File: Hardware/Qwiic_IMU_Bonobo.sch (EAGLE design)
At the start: 33 parts, among them J2 SMD, J3 PTH, J4 SMD, J6 SPI, U2 BNO080

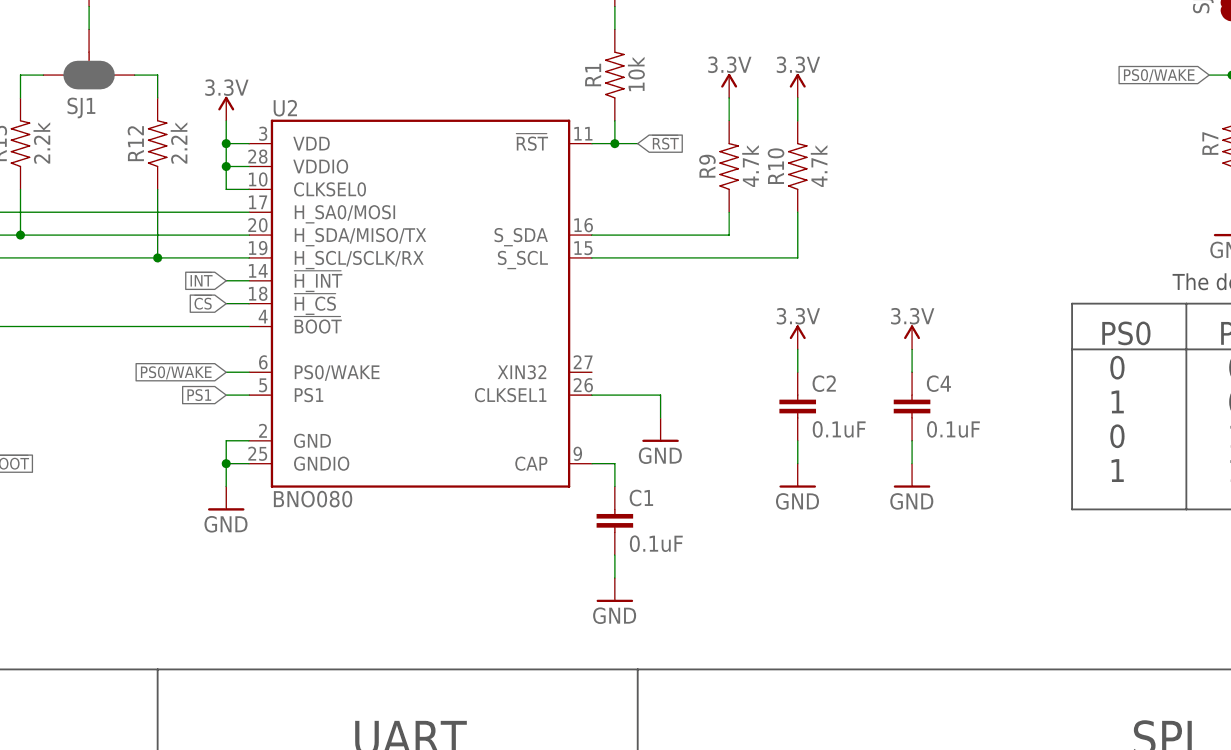
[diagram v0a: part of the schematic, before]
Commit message: Adding 32kHz xtal. Fixing UART silk.
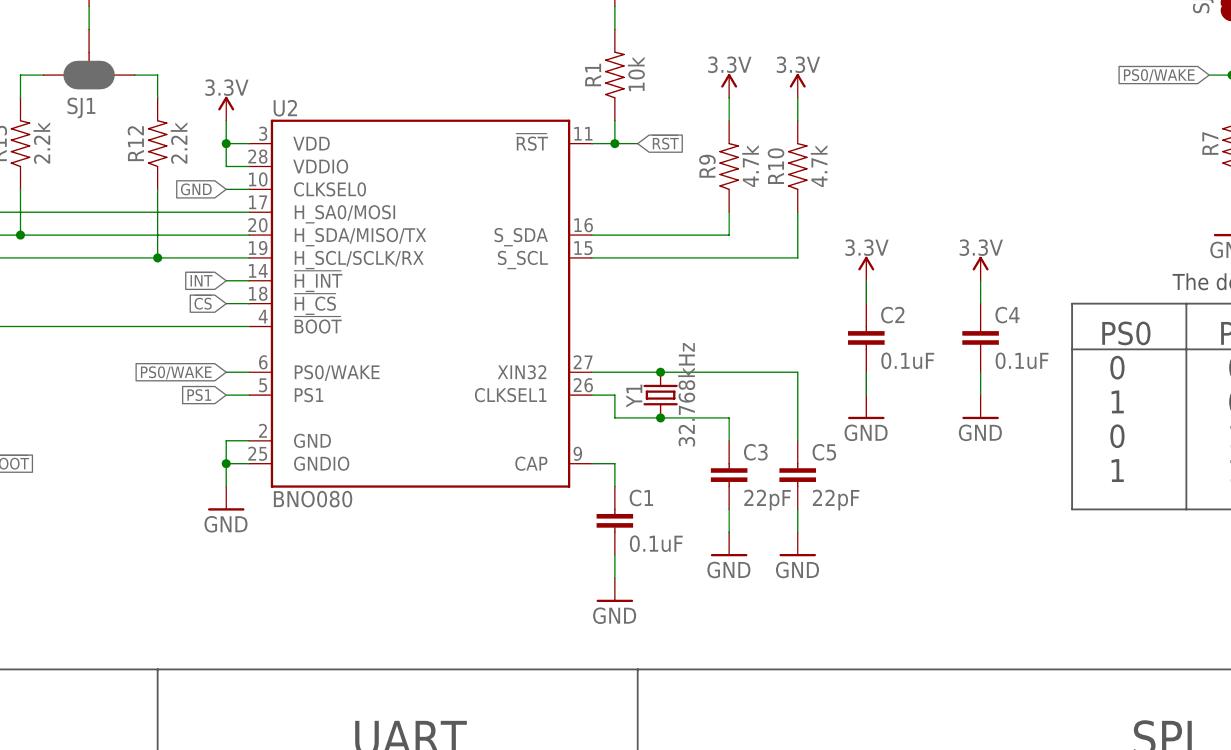
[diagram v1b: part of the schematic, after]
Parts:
- added C3, C5: 22pF, SparkFun-Capacitors:22PF-0603-50V-5%
- added Y1: 32.768kHz, SparkFun-Clocks:CRYSTAL-32.768KHZSMD-3.2X1.5
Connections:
- new net N$1: C5.1, U2.XIN32, Y1.2
- new net N$2: C3.1, U2.CLKSEL1, Y1.1
- net 3.3V: no longer U2.CLKSEL0
- net GND: now also C3.2, C5.2, U2.CLKSEL0; no longer U2.CLKSEL1
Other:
- moved on the sheet: C2, C4

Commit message: Label update. PWR LED added. Logo change.
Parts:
- removed U$1, U$2: SPARKX-LOGO3, SparkX:SPARKX-LOGO3
- added D1: RED, SparkFun-LED:LED-RED0603
- added LOGO4: SFE_LOGO_FLAME.1_INCH, SparkFun-Aesthetics:SFE_LOGO_FLAME.1_INCH
- added LOGO5: SFE_LOGO_NAME_FLAME.1_INCH, SparkFun-Aesthetics:SFE_LOGO_NAME_FLAME.1_INCH
- added R2: 1k, SparkFun-Resistors:1KOHM-0603-1/10W-1%
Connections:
- new net N$3: D1.C, R2.2
- net 3.3V: now also D1.A
- net GND: now also R2.1
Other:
- note added: "Power"
- moved on the sheet: R7, R8, SJ3, SJ4
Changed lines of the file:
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@@
 <part name="GND7" library="SparkFun" deviceset="GND" device=""/>
 <part name="FRAME1" library="SparkFun-Aesthetics" deviceset="FRAME-LETTER" device=""/>
-<part name="U$2" library="SparkX" deviceset="SPARKX-LOGO" device="3" value="SPARKX-LOGO3"/>
 <part name="C4" library="SparkFun-Capacitors" deviceset="0.1UF" device="-0603-25V-(+80/-20%)" value="0.1uF"/>
 <part name="SUPPLY8" library="SparkFun-PowerSymbols" deviceset="3.3V" device=""/>
@@
 <part name="GND8" library="SparkFun" deviceset="GND" device=""/>
 <part name="LOGO1" library="SparkFun-Aesthetics" deviceset="OSHW-LOGO" device="MINI"/>
-<part name="U$1" library="SparkX" deviceset="SPARKX-LOGO" device="3" value="SPARKX-LOGO3"/>
 <part name="U2" library="BNO080" deviceset="BNO080" device=""/>
 <part name="C1" library="SparkFun-Capacitors" deviceset="0.1UF" device="-0603-25V-(+80/-20%)" value="0.1uF"/>
@@
 <part name="C5" library="SparkFun-Capacitors" deviceset="22PF" device="-0603-50V-5%" value="22pF"/>
 <part name="GND14" library="SparkFun" deviceset="GND" device=""/>
+<part name="LOGO4" library="SparkFun-Aesthetics" deviceset="SFE_LOGO_FLAME" device=".1_INCH"/>
+<part name="LOGO5" library="SparkFun-Aesthetics" deviceset="SFE_LOGO_NAME_FLAME" device=".1_INCH"/>
+<part name="D1" library="SparkFun-LED" deviceset="LED-RED" device="0603" value="RED"/>
+<part name="SUPPLY3" library="SparkFun-PowerSymbols" deviceset="3.3V" device=""/>
+<part name="R2" library="SparkFun-Resistors" deviceset="1KOHM" device="-0603-1/10W-1%" value="1k"/>
+<part name="GND15" library="SparkFun" deviceset="GND" device=""/>
 </parts>
 <sheets>
@@
 <wire x1="147.32" y1="91.44" x2="147.32" y2="35.56" width="0.2032" layer="97"/>
 <wire x1="93.98" y1="91.44" x2="93.98" y2="0" width="0.2032" layer="97"/>
+<text x="240.792" y="159.258" size="1.778" layer="97" rot="R90">Power</text>
 </plain>
 <instances>
@@
 <instance part="FRAME1" gate="G$1" x="0" y="0"/>
 <instance part="FRAME1" gate="V" x="147.32" y="0"/>
-<instance part="U$2" gate="G$1" x="121.92" y="7.62"/>
 <instance part="C4" gate="G$1" x="185.42" y="127"/>
 <instance part="SUPPLY8" gate="G$1" x="66.04" y="43.18" rot="MR0"/>
@@
 <instance part="GND8" gate="1" x="66.04" y="27.94" rot="MR0"/>
 <instance part="LOGO1" gate="G$1" x="121.92" y="22.86"/>
-<instance part="U$1" gate="G$1" x="121.92" y="7.62"/>
 <instance part="U2" gate="U1" x="124.46" y="132.08"/>
 <instance part="C1" gate="G$1" x="144.78" y="106.68"/>
@@
 <instance part="R6" gate="G$1" x="58.42" y="149.86" rot="MR90"/>
 <instance part="SUPPLY11" gate="G$1" x="58.42" y="157.48" rot="MR0"/>
-<instance part="R7" gate="G$1" x="213.36" y="149.86" rot="R90"/>
-<instance part="SUPPLY12" gate="G$1" x="213.36" y="172.72"/>
-<instance part="R8" gate="G$1" x="228.6" y="149.86" rot="R90"/>
-<instance part="SUPPLY13" gate="G$1" x="228.6" y="172.72"/>
-<instance part="GND11" gate="1" x="213.36" y="139.7"/>
-<instance part="GND12" gate="1" x="228.6" y="139.7"/>
-<instance part="SJ3" gate="1" x="213.36" y="165.1" rot="MR270"/>
-<instance part="SJ4" gate="1" x="228.6" y="165.1" rot="MR270"/>
+<instance part="R7" gate="G$1" x="205.74" y="149.86" rot="R90"/>
+<instance part="SUPPLY12" gate="G$1" x="205.74" y="172.72"/>
+<instance part="R8" gate="G$1" x="220.98" y="149.86" rot="R90"/>
+<instance part="SUPPLY13" gate="G$1" x="220.98" y="172.72"/>
+<instance part="GND11" gate="1" x="205.74" y="139.7"/>
+<instance part="GND12" gate="1" x="220.98" y="139.7"/>
+<instance part="SJ3" gate="1" x="205.74" y="165.1" rot="MR270"/>
+<instance part="SJ4" gate="1" x="220.98" y="165.1" rot="MR270"/>
 <instance part="R9" gate="G$1" x="157.48" y="147.32" rot="R90"/>
 <instance part="R10" gate="G$1" x="165.1" y="147.32" rot="R90"/>
@@
 <instance part="C5" gate="G$1" x="165.1" y="111.76"/>
 <instance part="GND14" gate="1" x="165.1" y="104.14"/>
+<instance part="LOGO4" gate="G$1" x="99.06" y="20.32"/>
+<instance part="LOGO5" gate="G$1" x="17.78" y="0"/>
+<instance part="D1" gate="G$1" x="233.68" y="165.1"/>
+<instance part="SUPPLY3" gate="G$1" x="233.68" y="172.72"/>
+<instance part="R2" gate="G$1" x="233.68" y="149.86" rot="R90"/>
+<instance part="GND15" gate="1" x="233.68" y="139.7"/>
 </instances>
 <busses>
@@
 <pinref part="SJ3" gate="1" pin="1"/>
 <pinref part="SUPPLY12" gate="G$1" pin="3.3V"/>
-<wire x1="213.36" y1="172.72" x2="213.36" y2="170.18" width="0.1524" layer="91"/>
+<wire x1="205.74" y1="172.72" x2="205.74" y2="170.18" width="0.1524" layer="91"/>
 </segment>
 <segment>
 <pinref part="SJ4" gate="1" pin="1"/>
 <pinref part="SUPPLY13" gate="G$1" pin="3.3V"/>
-<wire x1="228.6" y1="172.72" x2="228.6" y2="170.18" width="0.1524" layer="91"/>
+<wire x1="220.98" y1="172.72" x2="220.98" y2="170.18" width="0.1524" layer="91"/>
 </segment>
 <segment>
@@
 <wire x1="205.74" y1="50.8" x2="205.74" y2="68.58" width="0.1524" layer="91"/>
 <pinref part="SUPPLY2" gate="G$1" pin="3.3V"/>
+</segment>
+<segment>
+<pinref part="D1" gate="G$1" pin="A"/>
+<pinref part="SUPPLY3" gate="G$1" pin="3.3V"/>
+<wire x1="233.68" y1="172.72" x2="233.68" y2="167.64" width="0.1524" layer="91"/>
 </segment>
 </net>
@@
 <pinref part="GND11" gate="1" pin="GND"/>
 <pinref part="R7" gate="G$1" pin="1"/>
-<wire x1="213.36" y1="144.78" x2="213.36" y2="142.24" width="0.1524" layer="91"/>
+<wire x1="205.74" y1="144.78" x2="205.74" y2="142.24" width="0.1524" layer="91"/>
 </segment>
 <segment>
 <pinref part="GND12" gate="1" pin="GND"/>
 <pinref part="R8" gate="G$1" pin="1"/>
-<wire x1="228.6" y1="144.78" x2="228.6" y2="142.24" width="0.1524" layer="91"/>
+<wire x1="220.98" y1="144.78" x2="220.98" y2="142.24" width="0.1524" layer="91"/>
 </segment>
 <segment>
@@
 <wire x1="104.14" y1="144.78" x2="101.6" y2="144.78" width="0.1524" layer="91"/>
 <label x="101.6" y="144.78" size="1.27" layer="95" rot="R180" xref="yes"/>
+</segment>
+<segment>
+<pinref part="R2" gate="G$1" pin="1"/>
+<pinref part="GND15" gate="1" pin="GND"/>
+<wire x1="233.68" y1="142.24" x2="233.68" y2="144.78" width="0.1524" layer="91"/>
 </segment>
 </net>
@@
 </segment>
 <segment>
-<label x="210.82" y="157.48" size="1.27" layer="95" rot="R180" xref="yes"/>
-<wire x1="210.82" y1="157.48" x2="213.36" y2="157.48" width="0.1524" layer="91"/>
+<label x="203.2" y="157.48" size="1.27" layer="95" rot="R180" xref="yes"/>
+<wire x1="203.2" y1="157.48" x2="205.74" y2="157.48" width="0.1524" layer="91"/>
 <pinref part="R7" gate="G$1" pin="2"/>
-<wire x1="213.36" y1="157.48" x2="213.36" y2="154.94" width="0.1524" layer="91"/>
+<wire x1="205.74" y1="157.48" x2="205.74" y2="154.94" width="0.1524" layer="91"/>
 <pinref part="SJ3" gate="1" pin="2"/>
-<wire x1="213.36" y1="157.48" x2="213.36" y2="160.02" width="0.1524" layer="91"/>
-<junction x="213.36" y="157.48"/>
+<wire x1="205.74" y1="157.48" x2="205.74" y2="160.02" width="0.1524" layer="91"/>
+<junction x="205.74" y="157.48"/>
 </segment>
 <segment>
@@
 </segment>
 <segment>
-<label x="226.06" y="157.48" size="1.27" layer="95" rot="R180" xref="yes"/>
-<wire x1="226.06" y1="157.48" x2="228.6" y2="157.48" width="0.1524" layer="91"/>
+<label x="218.44" y="157.48" size="1.27" layer="95" rot="R180" xref="yes"/>
+<wire x1="218.44" y1="157.48" x2="220.98" y2="157.48" width="0.1524" layer="91"/>
 <pinref part="R8" gate="G$1" pin="2"/>
-<wire x1="228.6" y1="157.48" x2="228.6" y2="154.94" width="0.1524" layer="91"/>
+<wire x1="220.98" y1="157.48" x2="220.98" y2="154.94" width="0.1524" layer="91"/>
 <pinref part="SJ4" gate="1" pin="2"/>
-<wire x1="228.6" y1="160.02" x2="228.6" y2="157.48" width="0.1524" layer="91"/>
-<junction x="228.6" y="157.48"/>
+<wire x1="220.98" y1="160.02" x2="220.98" y2="157.48" width="0.1524" layer="91"/>
+<junction x="220.98" y="157.48"/>
 </segment>
 <segment>
@@
 </segment>
 </net>
+<net name="N$3" class="0">
+<segment>
+<pinref part="D1" gate="G$1" pin="C"/>
+<pinref part="R2" gate="G$1" pin="2"/>
+<wire x1="233.68" y1="154.94" x2="233.68" y2="160.02" width="0.1524" layer="91"/>
+</segment>
+</net>
